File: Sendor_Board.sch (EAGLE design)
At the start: 26 parts, among them Q1 8.000Mhz, U1 PIC32MX795F512H-80I/PT, U2 SHT25, U3 MPL115A2, X1 MINI-USB-SHIELD-UX60A-MB-5ST

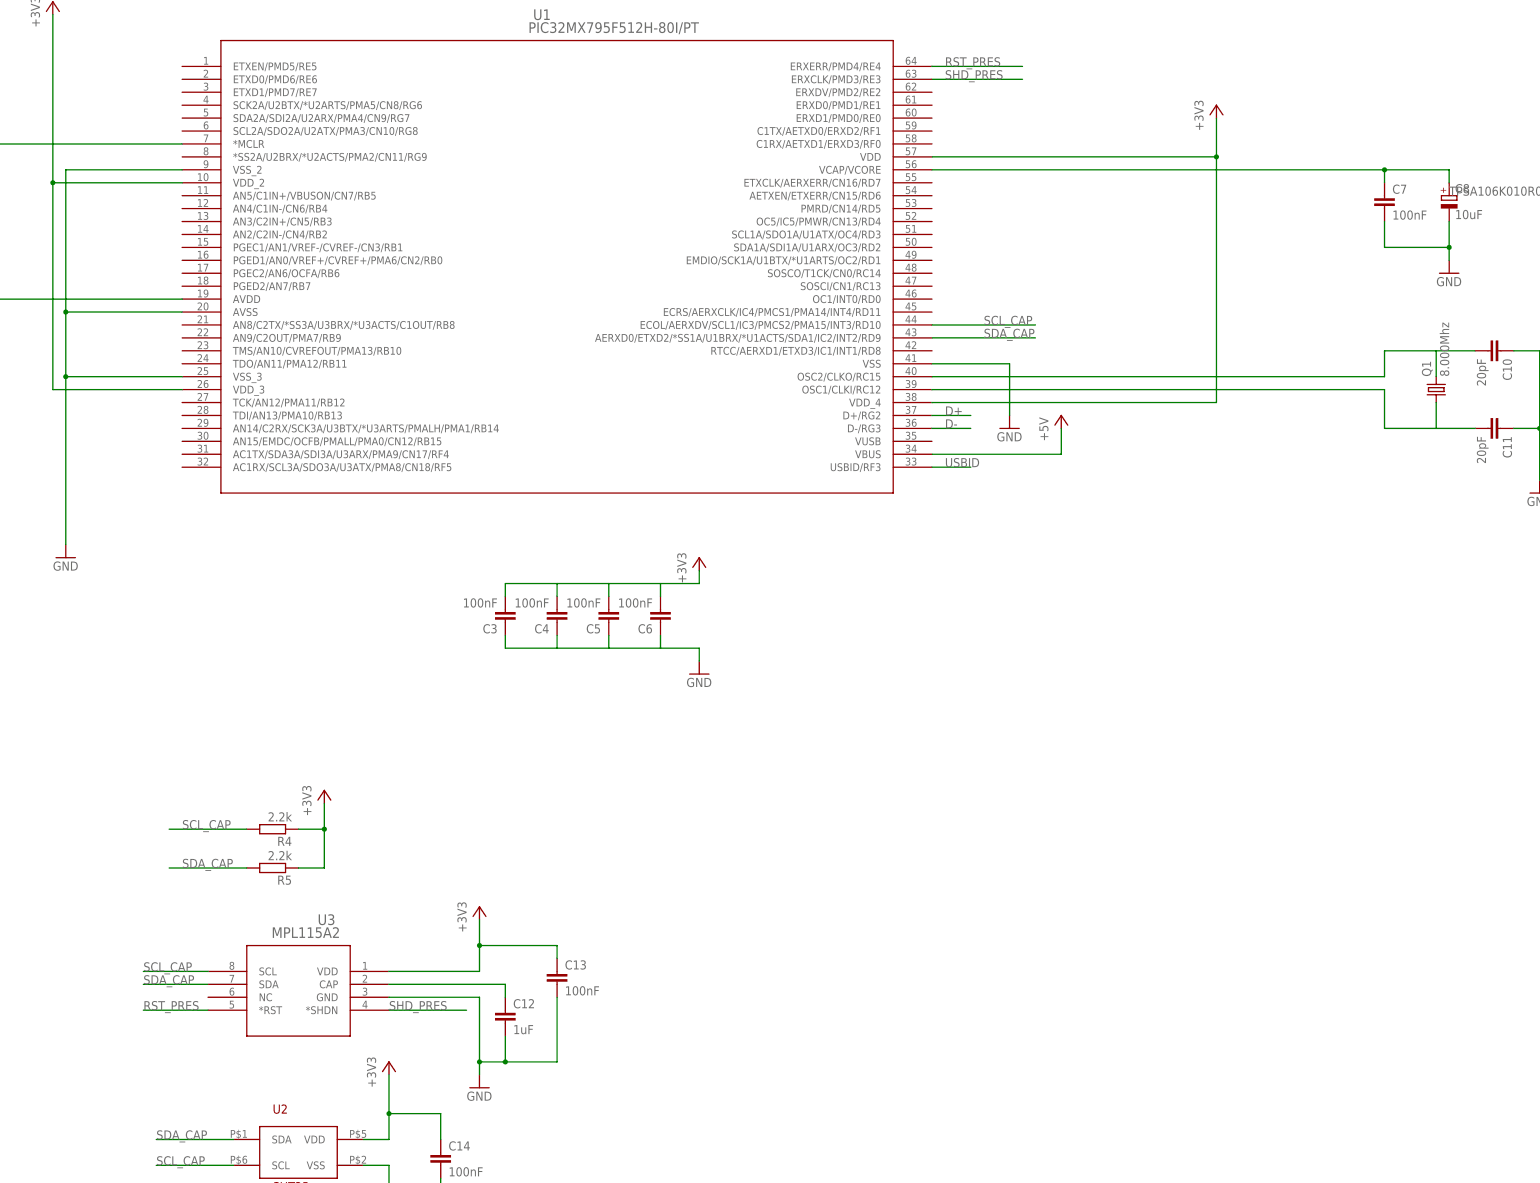
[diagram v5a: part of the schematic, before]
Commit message: Add MRF24J40MA to schematic
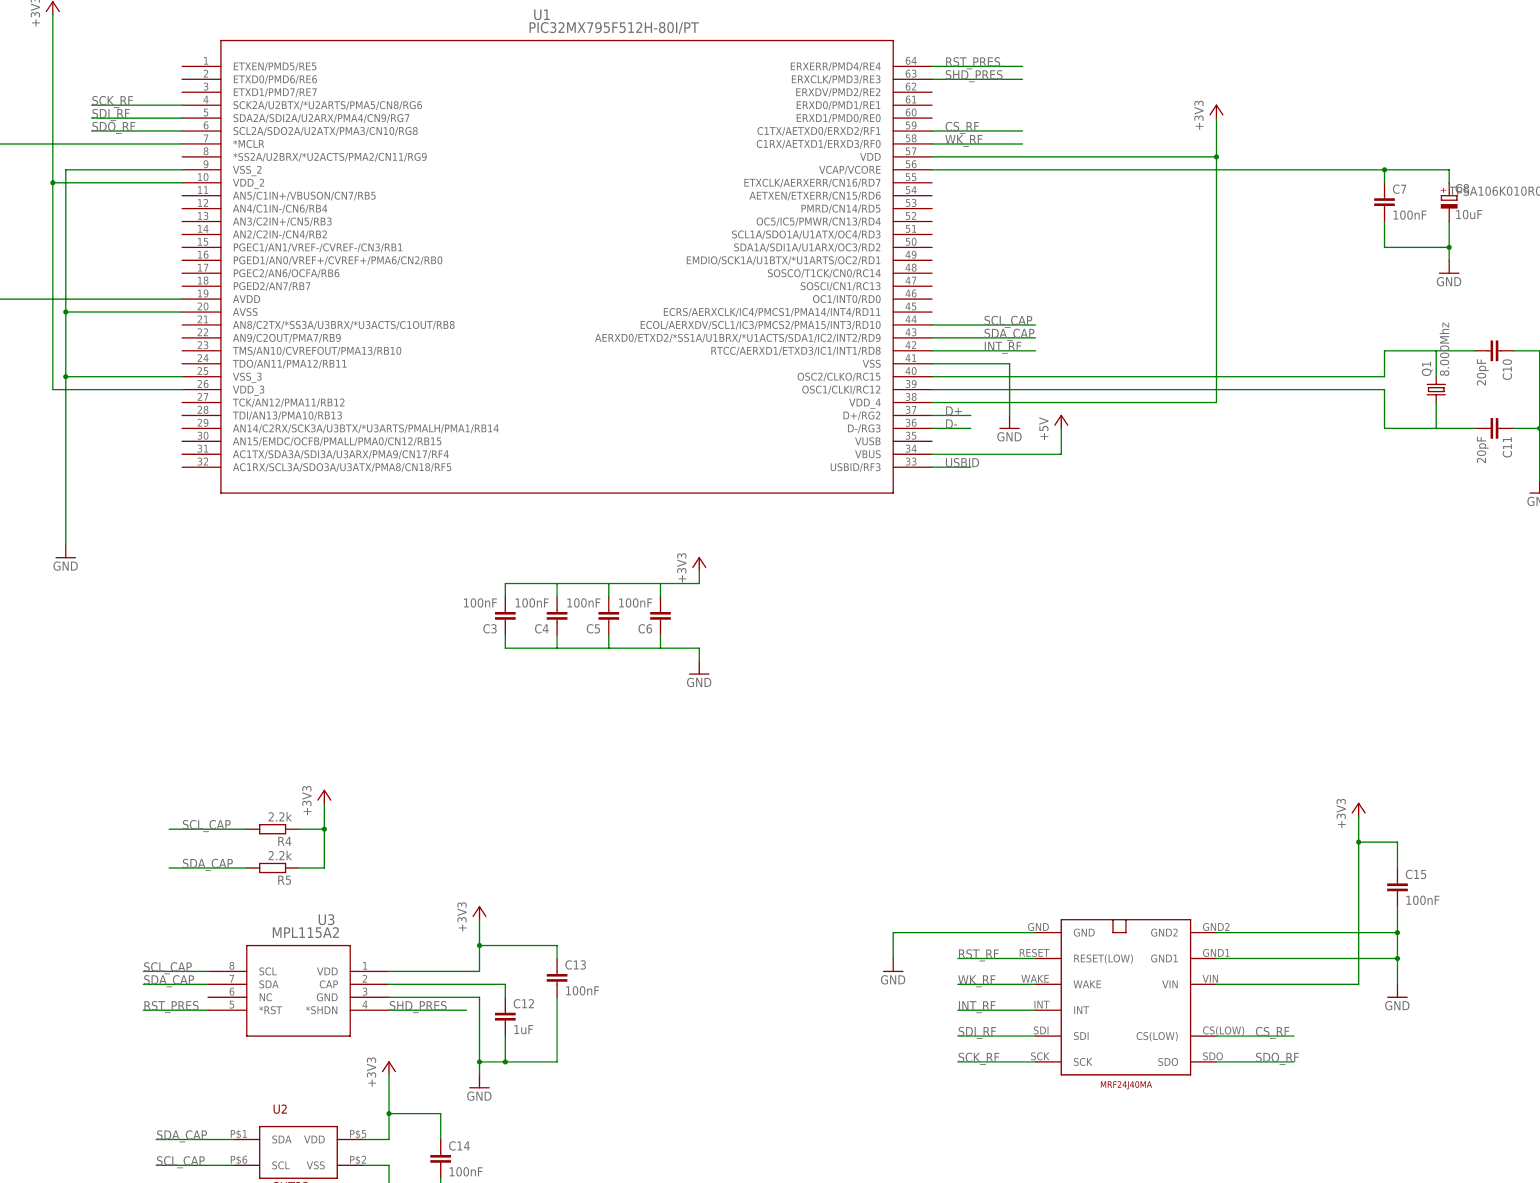
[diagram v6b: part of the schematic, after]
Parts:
- added C15: 100nF, resistor:C-EUC1206K
- added U4: MRF24J40MA, pfo:MRF24J40MA
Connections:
- new net CS_RF: U1.C1TX/AETXD0/ERXD2/RF1, U4.CS(LOW)
- new net INT_RF: U1.RTCC/AERXD1/ETXD3/IC1/INT1/RD8, U4.INT
- new net RST_RF: U4.RESET(LOW)
- new net SCK_RF: U1.SCK2A/U2BTX/*U2ARTS/PMA5/CN8/RG6, U4.SCK
- new net SDI_RF: U1.SDA2A/SDI2A/U2ARX/PMA4/CN9/RG7, U4.SDI
- new net SDO_RF: U1.SCL2A/SDO2A/U2ATX/PMA3/CN10/RG8, U4.SDO
- new net WK_RF: U1.C1RX/AETXD1/ERXD3/RF0, U4.WAKE
- net +3V3: now also C15.1, U4.VIN
- net GND: now also C15.2, U4.GND, U4.GND1, U4.GND2
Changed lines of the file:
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@@
 <part name="P+2" library="supply1" deviceset="+5V" device=""/>
 <part name="GND10" library="supply1" deviceset="GND" device=""/>
+<part name="U4" library="pfo" deviceset="MRF24J40MA" device=""/>
+<part name="GND11" library="supply1" deviceset="GND" device=""/>
+<part name="GND12" library="supply1" deviceset="GND" device=""/>
+<part name="+3V5" library="supply1" deviceset="+3V3" device=""/>
+<part name="C15" library="resistor" deviceset="C-EU" device="C1206K" value="100nF"/>
 </parts>
 <sheets>
@@
 <instance part="P+2" gate="1" x="172.72" y="15.24"/>
 <instance part="GND10" gate="1" x="-91.44" y="-86.36"/>
+<instance part="U4" gate="G$1" x="193.04" y="-91.44"/>
+<instance part="GND11" gate="1" x="238.76" y="-99.06"/>
+<instance part="GND12" gate="1" x="139.7" y="-93.98"/>
+<instance part="+3V5" gate="G$1" x="231.14" y="-60.96"/>
+<instance part="C15" gate="G$1" x="238.76" y="-76.2"/>
 </instances>
 <busses>
@@
 <junction x="58.42" y="-111.76"/>
 </segment>
+<segment>
+<pinref part="U4" gate="G$1" pin="GND"/>
+<pinref part="GND12" gate="1" pin="GND"/>
+<wire x1="167.64" y1="-86.36" x2="139.7" y2="-86.36" width="0.1524" layer="91"/>
+<wire x1="139.7" y1="-86.36" x2="139.7" y2="-91.44" width="0.1524" layer="91"/>
+</segment>
+<segment>
+<pinref part="U4" gate="G$1" pin="GND2"/>
+<pinref part="GND11" gate="1" pin="GND"/>
+<wire x1="203.2" y1="-86.36" x2="238.76" y2="-86.36" width="0.1524" layer="91"/>
+<wire x1="238.76" y1="-86.36" x2="238.76" y2="-91.44" width="0.1524" layer="91"/>
+<pinref part="U4" gate="G$1" pin="GND1"/>
+<wire x1="238.76" y1="-91.44" x2="238.76" y2="-96.52" width="0.1524" layer="91"/>
+<wire x1="203.2" y1="-91.44" x2="238.76" y2="-91.44" width="0.1524" layer="91"/>
+<junction x="238.76" y="-91.44"/>
+<pinref part="C15" gate="G$1" pin="2"/>
+<wire x1="238.76" y1="-81.28" x2="238.76" y2="-86.36" width="0.1524" layer="91"/>
+<junction x="238.76" y="-86.36"/>
+</segment>
 </net>
 <net name="+3V3" class="0">
@@
 <junction x="58.42" y="-88.9"/>
 </segment>
+<segment>
+<pinref part="U4" gate="G$1" pin="VIN"/>
+<pinref part="+3V5" gate="G$1" pin="+3V3"/>
+<wire x1="203.2" y1="-96.52" x2="231.14" y2="-96.52" width="0.1524" layer="91"/>
+<wire x1="231.14" y1="-96.52" x2="231.14" y2="-68.58" width="0.1524" layer="91"/>
+<pinref part="C15" gate="G$1" pin="1"/>
+<wire x1="231.14" y1="-68.58" x2="231.14" y2="-63.5" width="0.1524" layer="91"/>
+<wire x1="238.76" y1="-73.66" x2="238.76" y2="-68.58" width="0.1524" layer="91"/>
+<wire x1="238.76" y1="-68.58" x2="231.14" y2="-68.58" width="0.1524" layer="91"/>
+<junction x="231.14" y="-68.58"/>
+</segment>
 </net>
 <net name="N$1" class="0">
@@
 </segment>
 </net>
+<net name="RST_RF" class="0">
+<segment>
+<pinref part="U4" gate="G$1" pin="RESET(LOW)"/>
+<wire x1="167.64" y1="-91.44" x2="152.4" y2="-91.44" width="0.1524" layer="91"/>
+<label x="152.4" y="-91.44" size="1.778" layer="95"/>
+</segment>
+</net>
+<net name="WK_RF" class="0">
+<segment>
+<pinref part="U4" gate="G$1" pin="WAKE"/>
+<wire x1="167.64" y1="-96.52" x2="152.4" y2="-96.52" width="0.1524" layer="91"/>
+<label x="152.4" y="-96.52" size="1.778" layer="95"/>
+</segment>
+<segment>
+<pinref part="U1" gate="A" pin="C1RX/AETXD1/ERXD3/RF0"/>
+<wire x1="147.32" y1="68.58" x2="165.1" y2="68.58" width="0.1524" layer="91"/>
+<label x="149.86" y="68.58" size="1.778" layer="95"/>
+</segment>
+</net>
+<net name="INT_RF" class="0">
+<segment>
+<pinref part="U4" gate="G$1" pin="INT"/>
+<wire x1="167.64" y1="-101.6" x2="152.4" y2="-101.6" width="0.1524" layer="91"/>
+<label x="152.4" y="-101.6" size="1.778" layer="95"/>
+</segment>
+<segment>
+<pinref part="U1" gate="A" pin="RTCC/AERXD1/ETXD3/IC1/INT1/RD8"/>
+<wire x1="147.32" y1="27.94" x2="167.64" y2="27.94" width="0.1524" layer="91"/>
+<label x="157.48" y="27.94" size="1.778" layer="95"/>
+</segment>
+</net>
+<net name="SDI_RF" class="0">
+<segment>
+<pinref part="U4" gate="G$1" pin="SDI"/>
+<wire x1="167.64" y1="-106.68" x2="152.4" y2="-106.68" width="0.1524" layer="91"/>
+<label x="152.4" y="-106.68" size="1.778" layer="95"/>
+</segment>
+<segment>
+<pinref part="U1" gate="A" pin="SDA2A/SDI2A/U2ARX/PMA4/CN9/RG7"/>
+<wire x1="0" y1="73.66" x2="-17.78" y2="73.66" width="0.1524" layer="91"/>
+<label x="-17.78" y="73.66" size="1.778" layer="95"/>
+</segment>
+</net>
+<net name="SCK_RF" class="0">
+<segment>
+<pinref part="U4" gate="G$1" pin="SCK"/>
+<wire x1="167.64" y1="-111.76" x2="152.4" y2="-111.76" width="0.1524" layer="91"/>
+<label x="152.4" y="-111.76" size="1.778" layer="95"/>
+</segment>
+<segment>
+<pinref part="U1" gate="A" pin="SCK2A/U2BTX/*U2ARTS/PMA5/CN8/RG6"/>
+<wire x1="0" y1="76.2" x2="-17.78" y2="76.2" width="0.1524" layer="91"/>
+<label x="-17.78" y="76.2" size="1.778" layer="95"/>
+</segment>
+</net>
+<net name="CS_RF" class="0">
+<segment>
+<pinref part="U4" gate="G$1" pin="CS(LOW)"/>
+<wire x1="203.2" y1="-106.68" x2="218.44" y2="-106.68" width="0.1524" layer="91"/>
+<label x="210.82" y="-106.68" size="1.778" layer="95"/>
+</segment>
+<segment>
+<pinref part="U1" gate="A" pin="C1TX/AETXD0/ERXD2/RF1"/>
+<wire x1="147.32" y1="71.12" x2="165.1" y2="71.12" width="0.1524" layer="91"/>
+<label x="149.86" y="71.12" size="1.778" layer="95"/>
+</segment>
+</net>
+<net name="SDO_RF" class="0">
+<segment>
+<pinref part="U4" gate="G$1" pin="SDO"/>
+<wire x1="203.2" y1="-111.76" x2="218.44" y2="-111.76" width="0.1524" layer="91"/>
+<label x="210.82" y="-111.76" size="1.778" layer="95"/>
+</segment>
+<segment>
+<pinref part="U1" gate="A" pin="SCL2A/SDO2A/U2ATX/PMA3/CN10/RG8"/>
+<wire x1="0" y1="71.12" x2="-17.78" y2="71.12" width="0.1524" layer="91"/>
+<label x="-17.78" y="71.12" size="1.778" layer="95"/>
+</segment>
+</net>

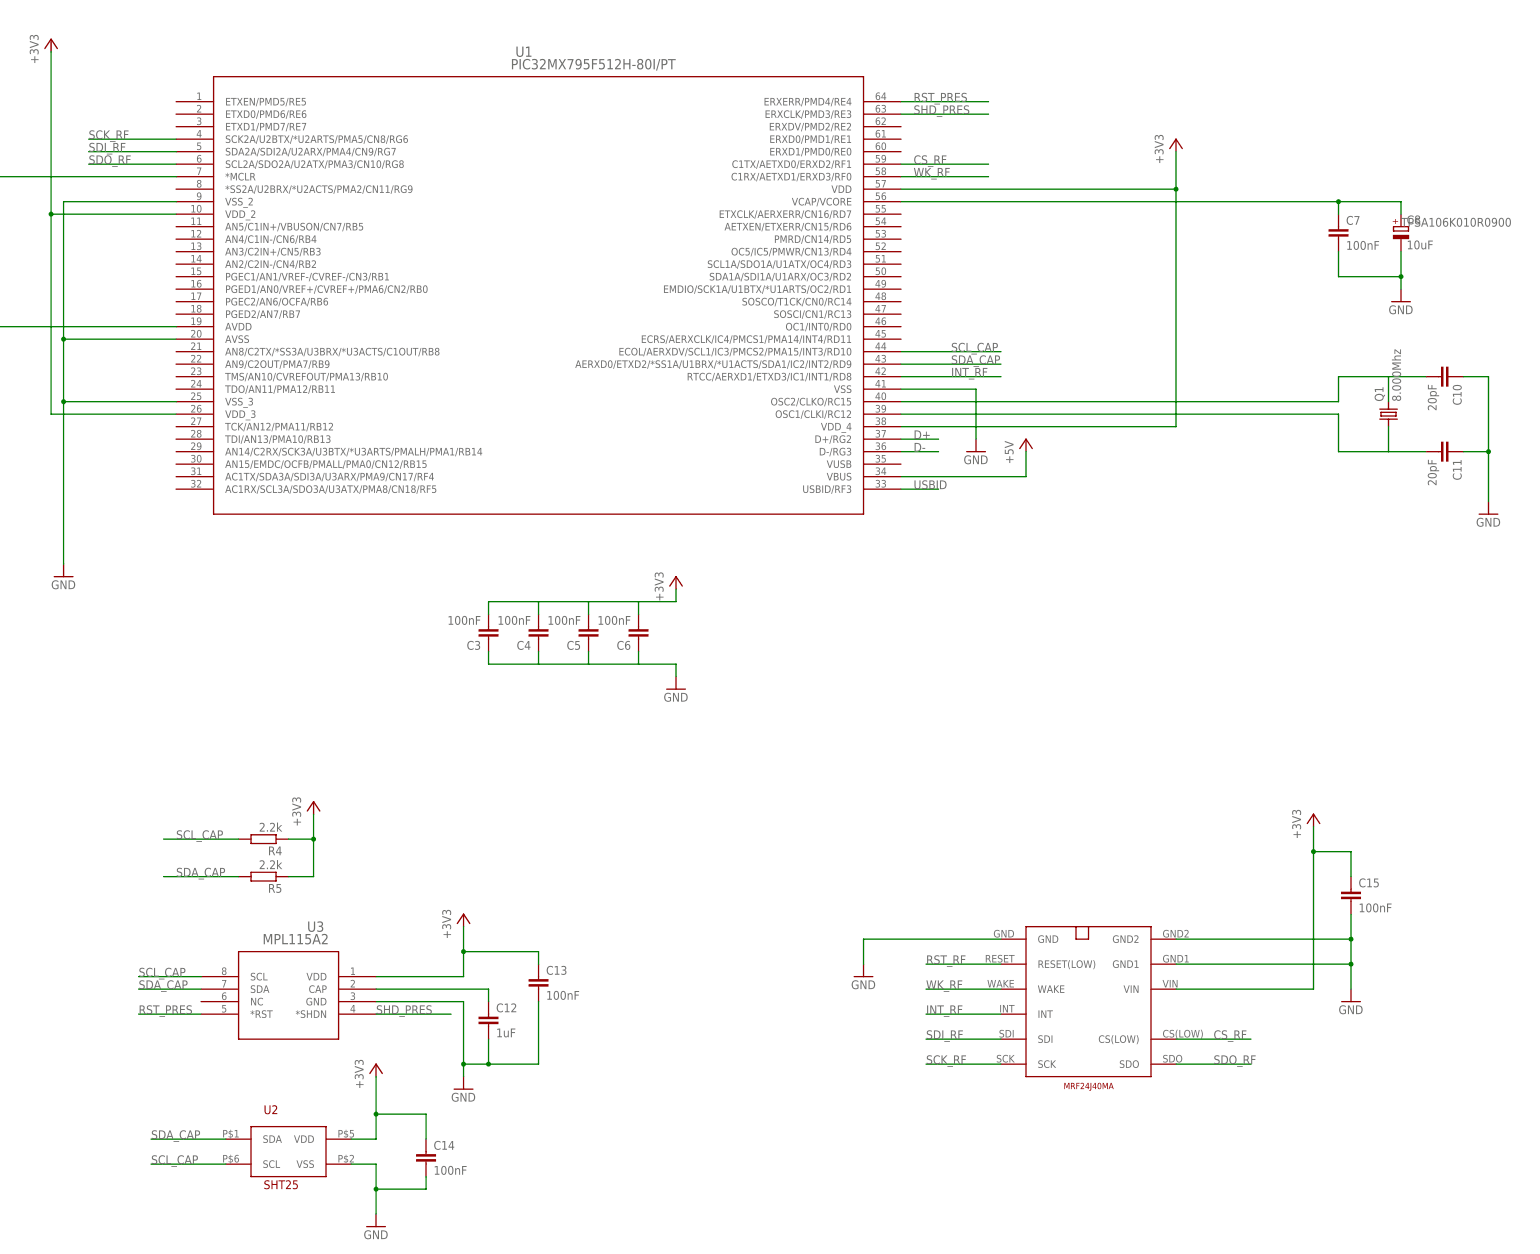
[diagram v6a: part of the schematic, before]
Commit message: Add electric radiator pilot function
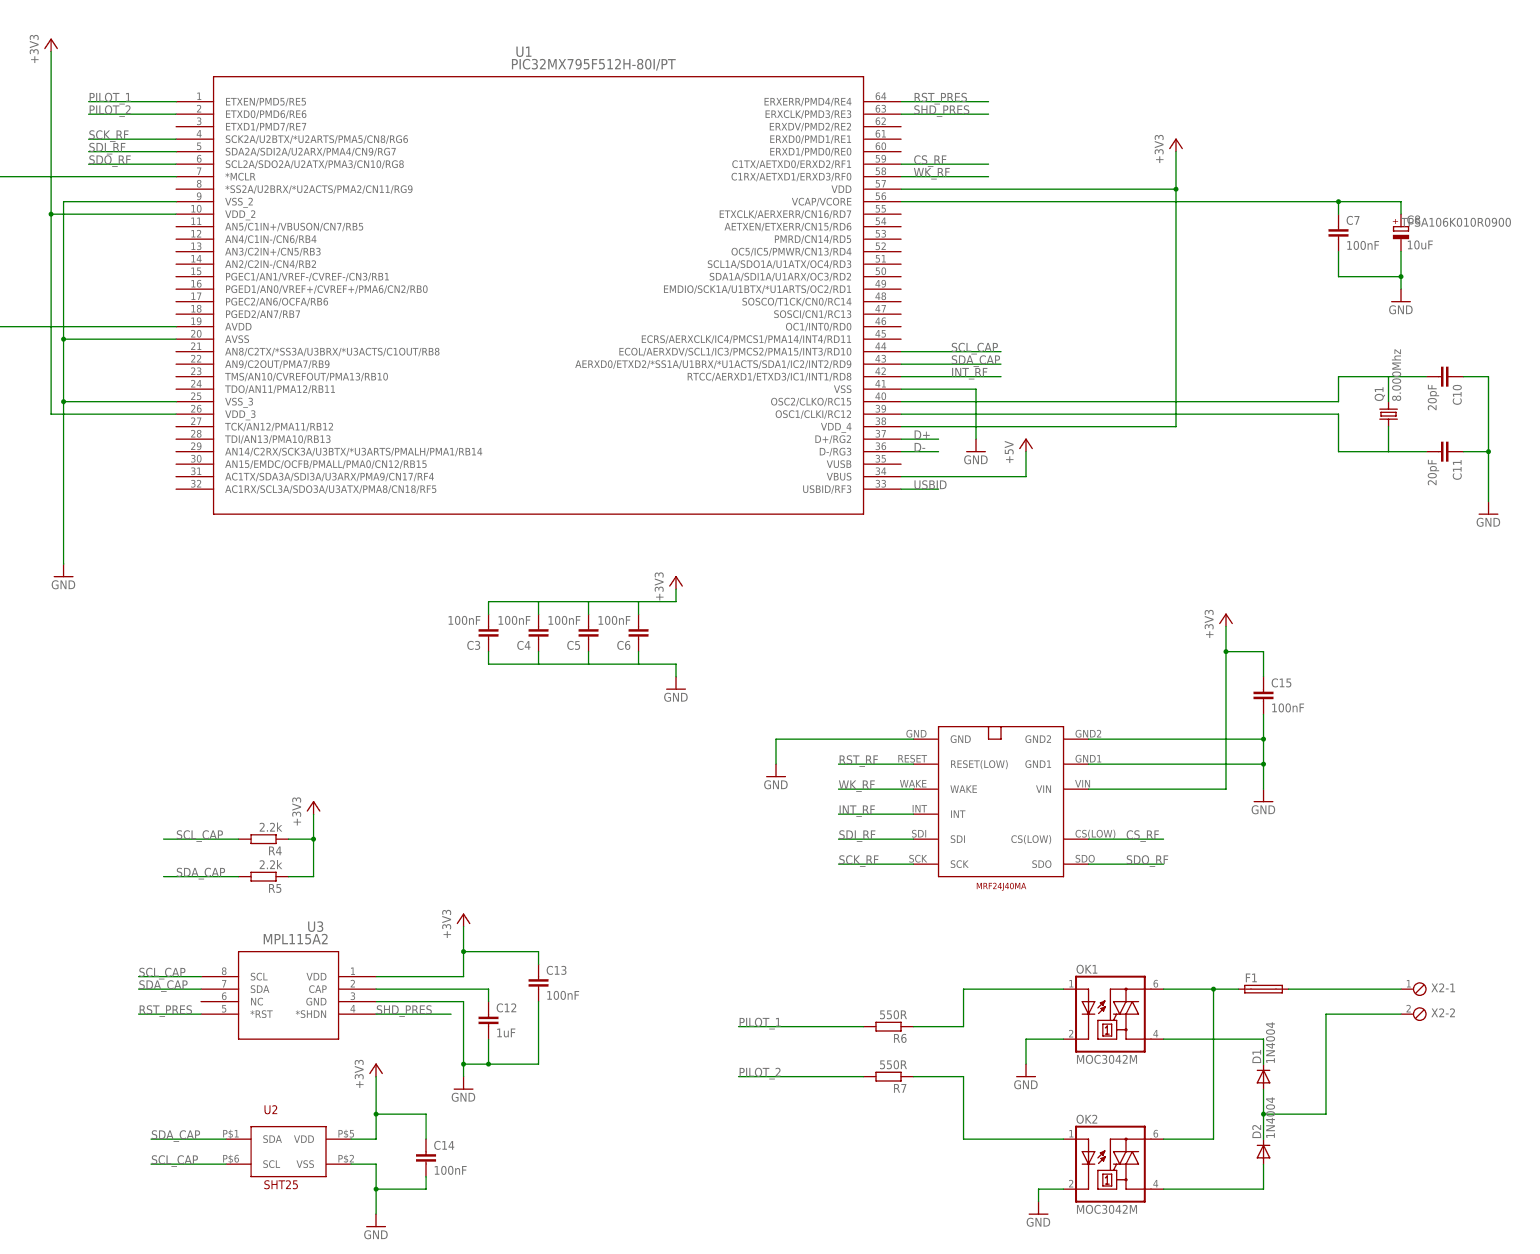
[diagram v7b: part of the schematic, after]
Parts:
- added D1, D2: 1N4004, diode:1N4004
- added F1: (no value), fuse:SH22,5
- added OK1, OK2: MOC3042M, optocoupler:MOC3042M
- added R6, R7: 550R, resistor:R-EU_R1206
- added X2: (no value), con-phoenix-254:MPT2
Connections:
- new net N$10: F1.1, OK1.A2, OK2.A2
- new net N$11: F1.2, X2-1.1
- new net N$12: D1.C, OK1.A1
- new net N$14: D2.A, OK2.A1
- new net N$15: D1.A, D2.C, X2-2.1
- new net N$8: OK1.A, R6.1
- new net N$9: OK2.A, R7.1
- new net PILOT_1: R6.2, U1.ETXEN/PMD5/RE5
- new net PILOT_2: R7.2, U1.ETXD0/PMD6/RE6
- net GND: now also OK1.C, OK2.C
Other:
- moved on the sheet: C15
